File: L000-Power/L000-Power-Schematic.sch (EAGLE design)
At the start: 59 parts, among them IC1 LM7805, IC2 LM7905, IC3 LM7809, IC4 LM7909, X1 JST-XH-2PIN, X10 JST-XH-5PIN, X11 JST-XH-5PIN, X12 JST-XH-5PIN, X13 JST-XH-5PIN, X14 JST-XH-5PIN, X15 JST-XH-5PIN, X16 JST-XH-5PIN, X17 JST-XH-5PIN, X18 JST-XH-5PIN, X19 JST-XH-5PIN, X2 JST-XH-5PIN, X20 JST-XH-5PIN, X21 JST-XH-5PIN, X3 JST-XH-5PIN, X4 JST-XH-5PIN, X5 JST-XH-5PIN, X6 JST-XH-5PIN, X7 JST-XH-5PIN, X8 JST-XH-5PIN, X9 JST-XH-5PIN

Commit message: Power
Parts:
- added R5, R6, R7, R8: 10k, resistor:R-US_0309/10
- C13, C14, C15, C16, C17, C18, C19, C20: device resistor:CPOL-USE5-13 -> rcl:CPOL-USE2,5-6E
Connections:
- new net X1: R8.2
- new net X2: R5.2
- new net X3: R6.2
- new net X4: R7.2
- net 5V+: now also C15.+; no longer C14.+
- net 9V+: now also C19.+; no longer C18.+
- net GND: now also C14.+, C15.-, C18.+, C19.-, R5.1, R6.1, R7.1, R8.1; no longer C14.-, C15.+, C18.-, C19.+
- net N$1: now also C14.-, C18.-; no longer C15.-, C19.-
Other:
- moved on the sheet: C14, C15, C18, C19

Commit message: Power
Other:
- note added: "Panel GND bus"
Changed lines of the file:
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@@
 <sheet>
 <plain>
+<text x="-38.1" y="-99.06" size="1.778" layer="91">Panel GND bus</text>
 </plain>
 <instances>

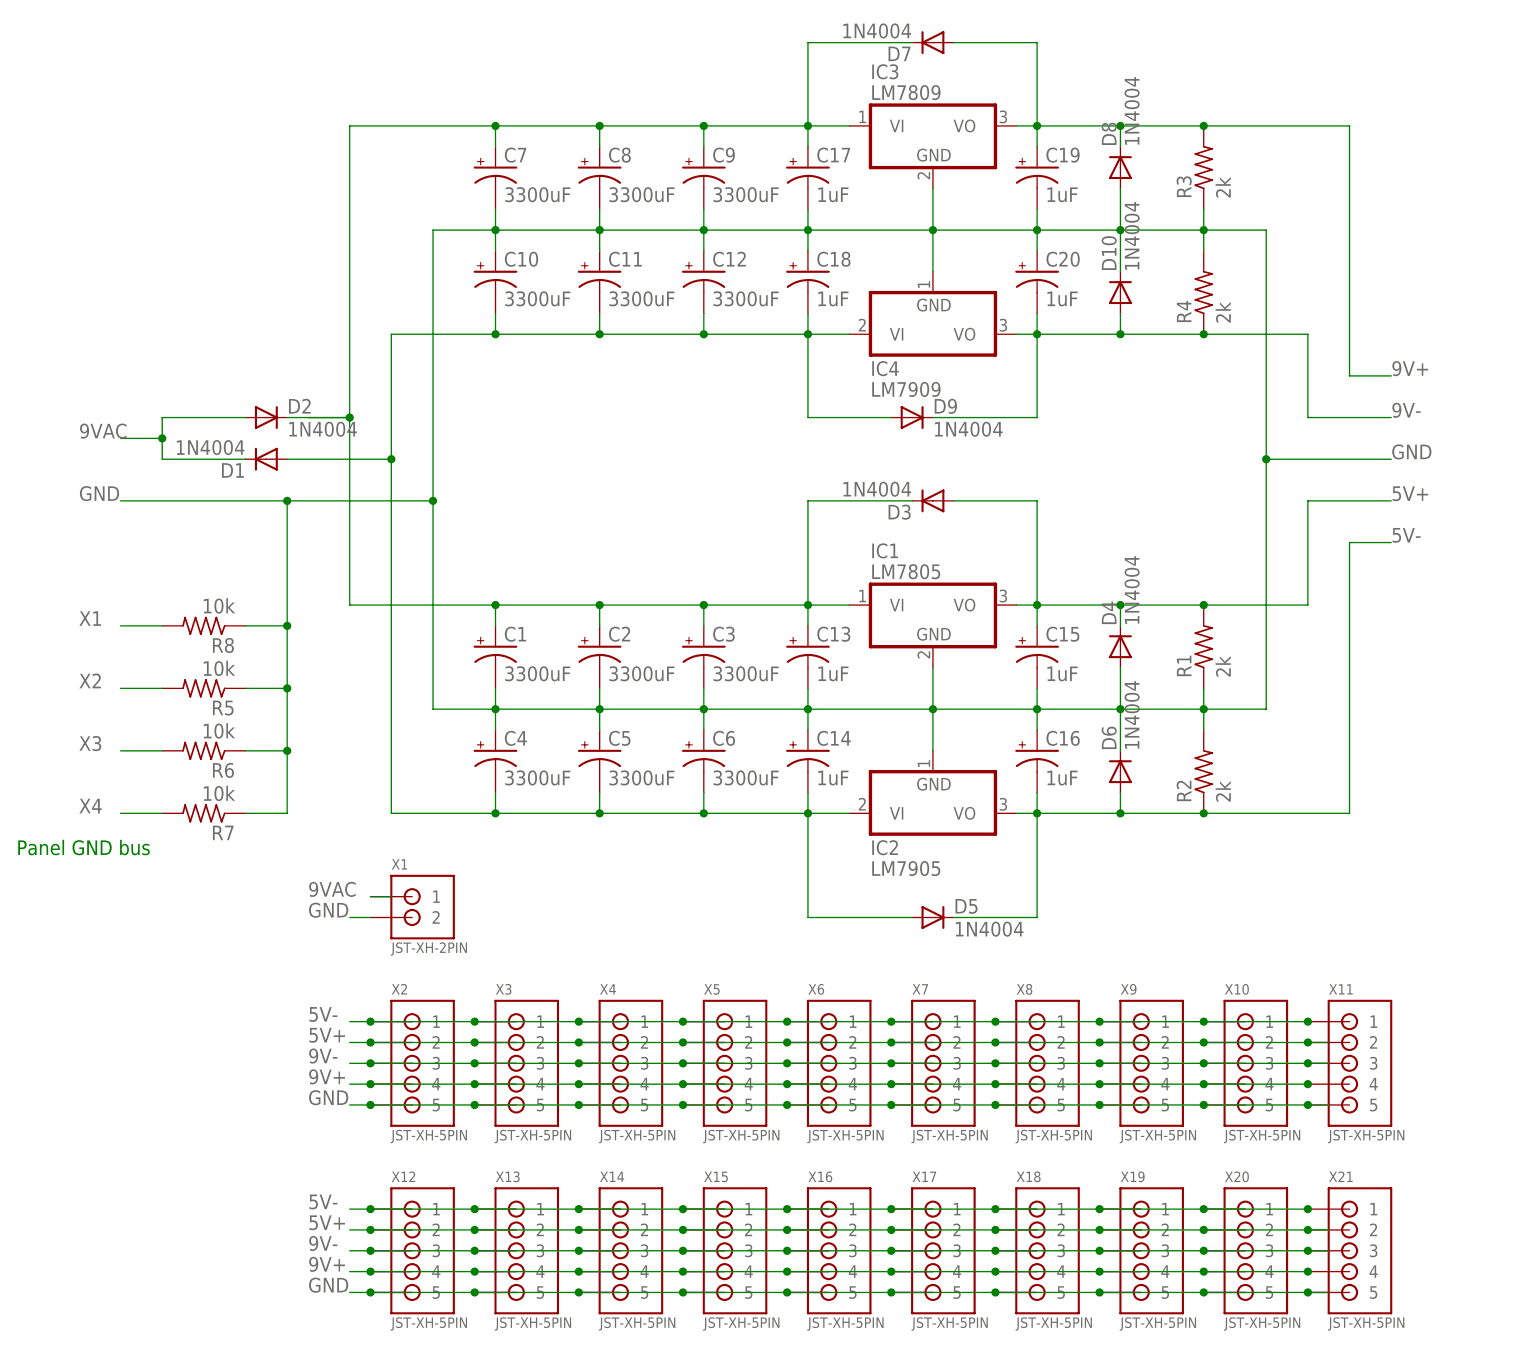
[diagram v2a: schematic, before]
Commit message: Add LEDs
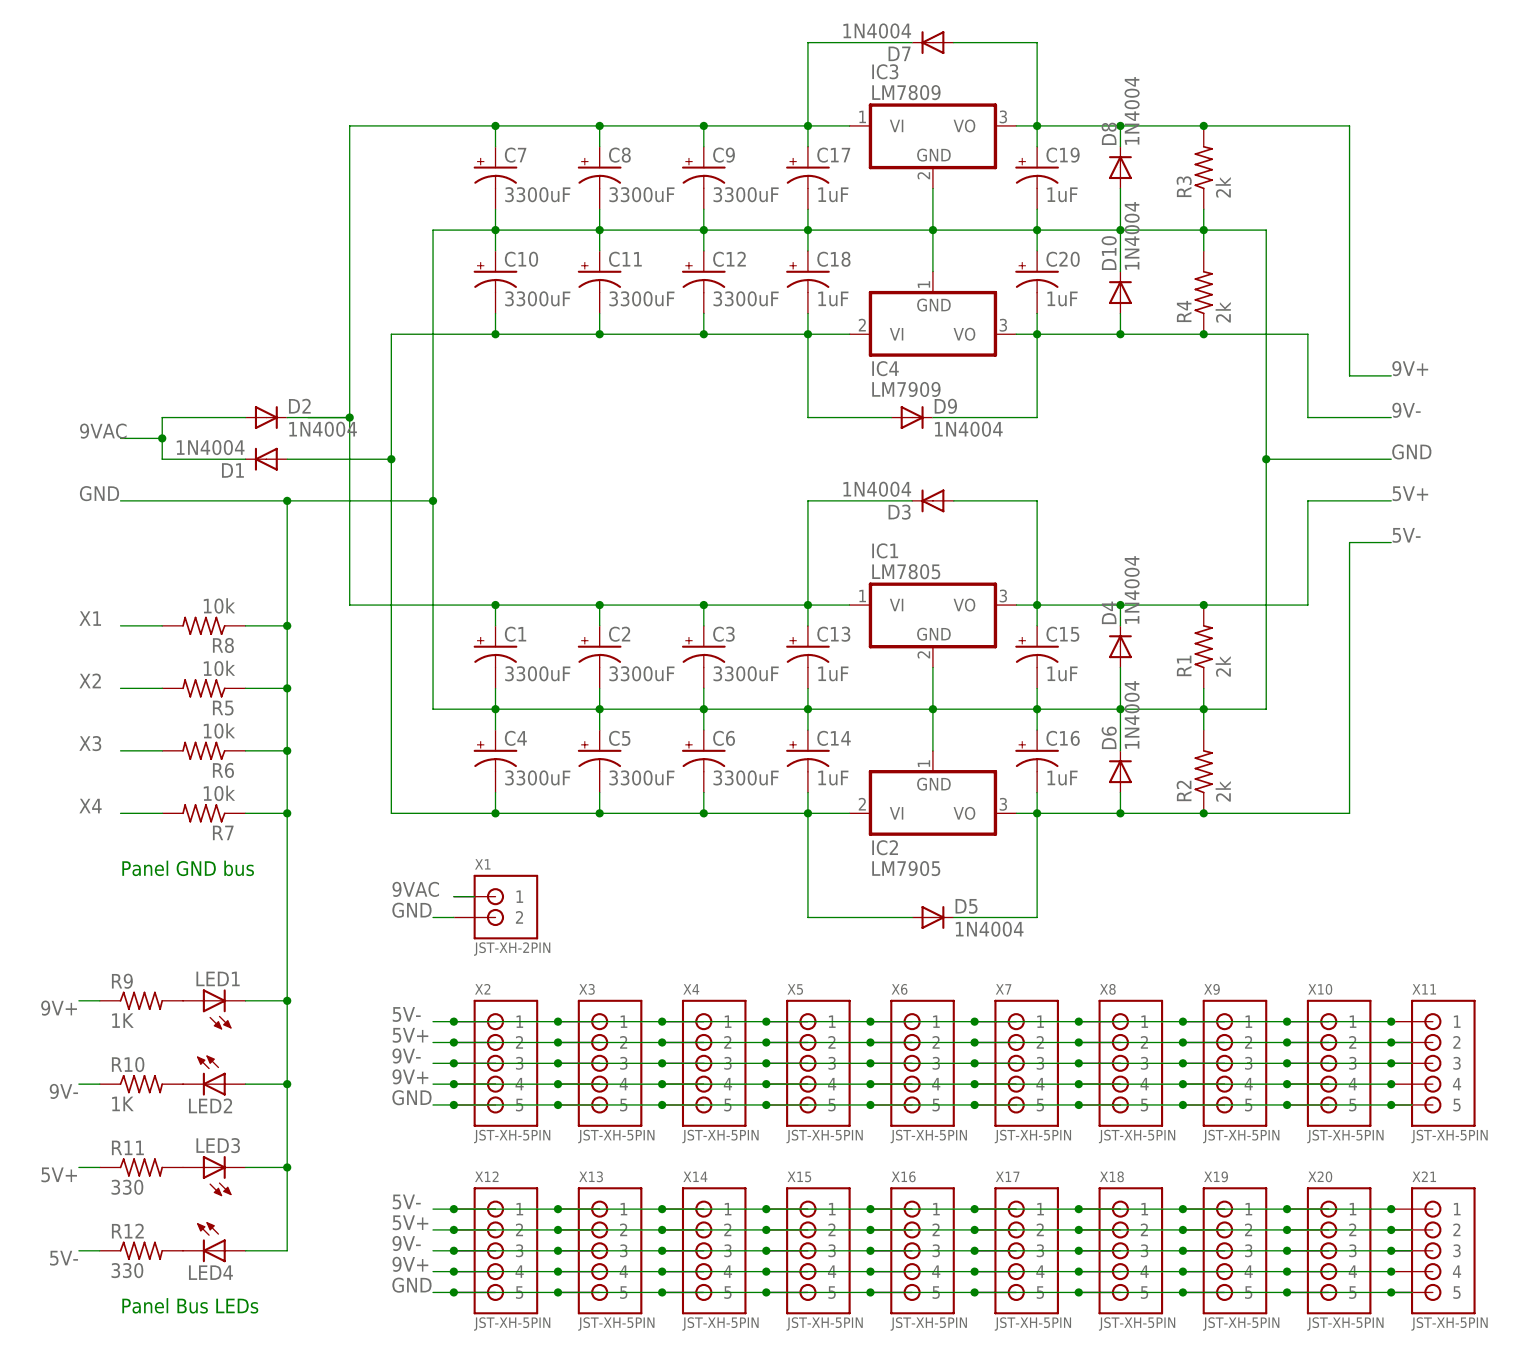
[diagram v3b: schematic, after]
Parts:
- added LED1, LED2, LED3, LED4: (no value), led:LED5MM
- added R10, R9: 1K, resistor:R-US_0309/10
- added R11, R12: 330, resistor:R-US_0309/10
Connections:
- new net N$2: LED3.A, R11.2
- new net N$3: LED4.C, R12.2
- new net N$4: LED1.A, R9.2
- new net N$5: LED2.C, R10.2
- net 5V+: now also R11.1
- net 5V-: now also R12.1
- net 9V+: now also R9.1
- net 9V-: now also R10.1
- net GND: now also LED1.C, LED2.A, LED3.C, LED4.A
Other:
- note added: "Panel Bus LEDs"
- moved on the sheet: X1, X10, X11, X12, X13, X14, X15, X16, X17, X18, X19, X2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

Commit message: FIX V2
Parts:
- removed C15, C16, C17, C18, C19, C20: 1uF, rcl:CPOL-USE2,5-6E
- removed R5, R6, R7, R8: 10k, resistor:R-US_0309/10
- C10, C11, C12, C7, C8, C9: value 3300uF -> 1uF; device resistor:CPOL-USE5-13 -> rcl:CPOL-USE2,5-6E
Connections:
- removed net N$1: C10.-, C11.-, C12.-, C14.-, C18.-, C4.-, C5.-, C6.-, D1.A, D5.A, D9.A, IC2.VI, IC4.VI
- removed net N$8: C1.+, C13.+, C17.+, C2.+, C3.+, C7.+, C8.+, C9.+, D2.C, D3.C, D7.C, IC1.VI, IC3.VI
- removed net X1: R8.2
- removed net X2: R5.2
- removed net X3: R6.2
- removed net X4: R7.2
- new net N$14: C13.-, C4.-, C5.-, C6.-, C9.-, D5.A, D9.A, IC2.VI, IC4.VI
- new net N$7: C1.+, C11.+, C2.+, C3.+, C7.+, D2.C, D3.C, D7.C, IC1.VI, IC3.VI
- net 5V+: now also C12.+; no longer C15.+
- net 5V-: now also C14.-; no longer C16.-
- net 9V+: now also C8.+; no longer C19.+
- net 9V-: now also C10.-; no longer C20.-
- net GND: now also C11.-, C12.-, C13.+, C9.+; no longer C11.+, C12.+, C13.-, C15.-, C16.+, C17.-, C18.+, C19.-, C20.+, C9.-, R5.1, R6.1, R7.1, R8.1
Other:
- note added: "X1"
- note added: "X2"
- note added: "X3"
- note added: "X4"
- moved on the sheet: C1, C10, C11, C12, C13, C14, C2, C3, C4, C5, C6, C7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

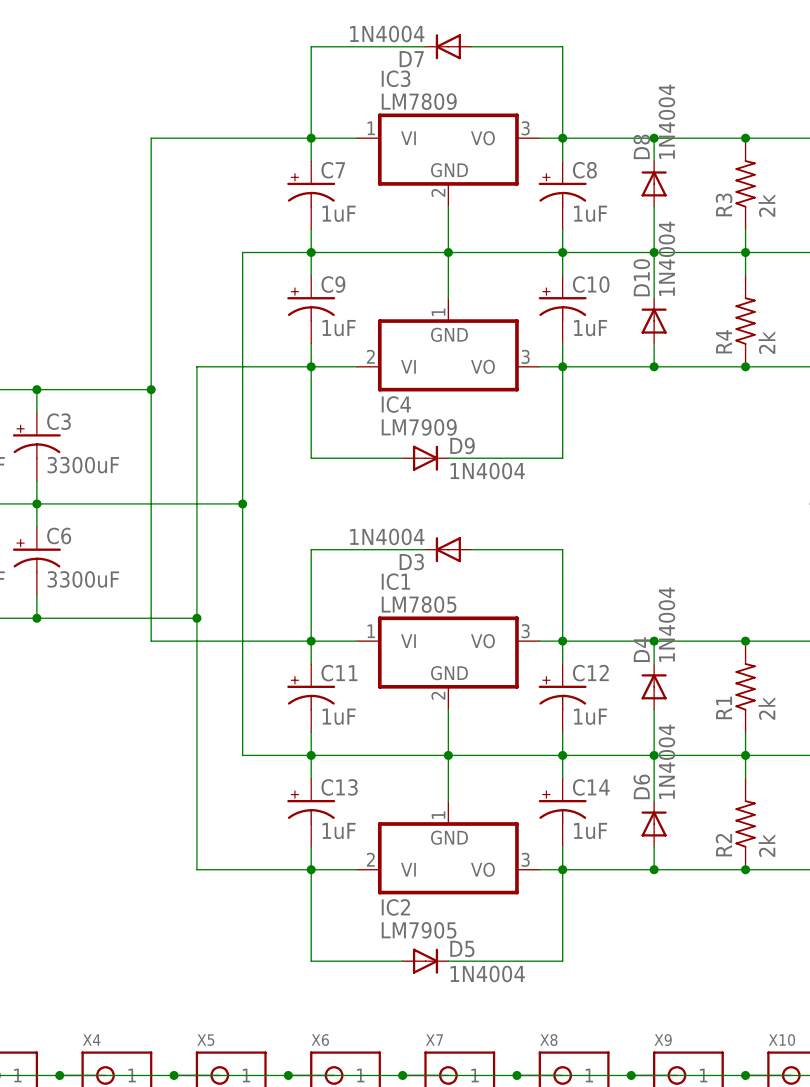
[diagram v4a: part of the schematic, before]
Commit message: POWER
Updated schematic and start of strip board
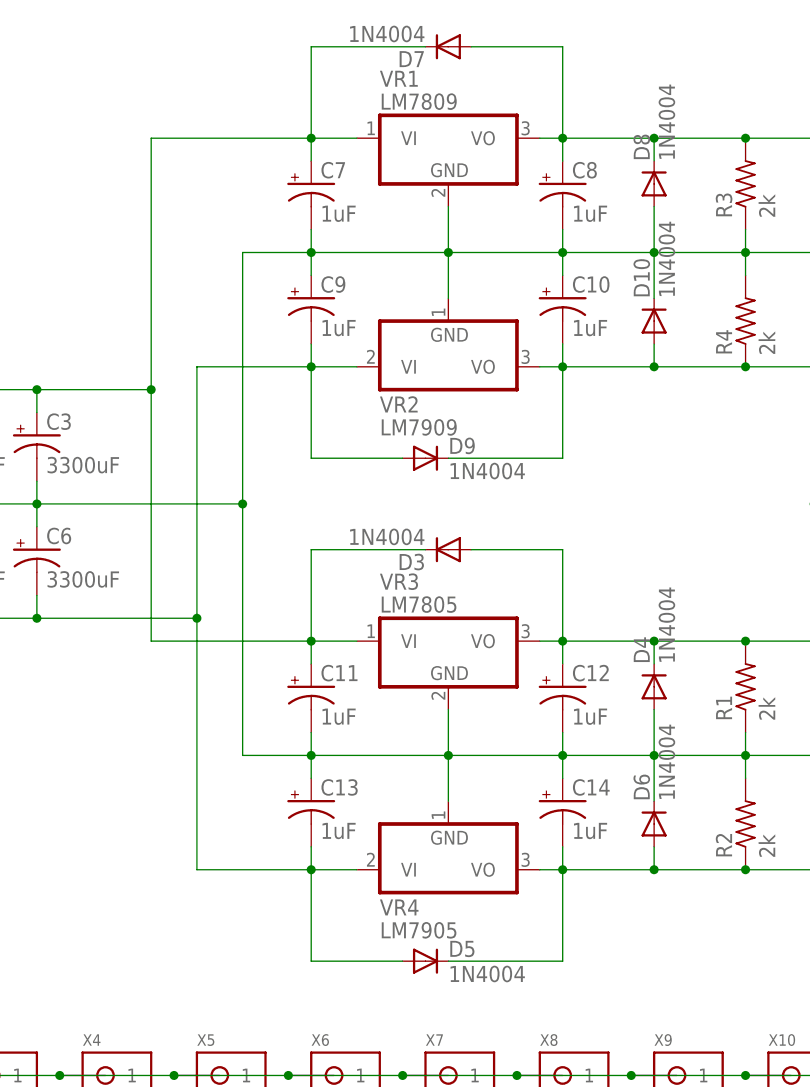
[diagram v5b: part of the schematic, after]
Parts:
- renumbered IC1 to VR3, IC2 to VR4, IC3 to VR1, IC4 to VR2
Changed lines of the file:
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@@
 <part name="C5" library="resistor" deviceset="CPOL-US" device="E5-13" value="3300uF"/>
 <part name="C6" library="resistor" deviceset="CPOL-US" device="E5-13" value="3300uF"/>
-<part name="IC1" library="linear" deviceset="78*" device="T" technology="05" value="LM7805"/>
+<part name="VR3" library="linear" deviceset="78*" device="T" technology="05" value="LM7805"/>
 <part name="D1" library="diode" deviceset="1N4004" device=""/>
 <part name="D2" library="diode" deviceset="1N4004" device=""/>
@@
 <part name="D5" library="diode" deviceset="1N4004" device=""/>
 <part name="D6" library="diode" deviceset="1N4004" device=""/>
-<part name="IC2" library="linear" deviceset="79*" device="T" technology="05" value="LM7905"/>
-<part name="IC3" library="linear" deviceset="78*" device="T" technology="08" value="LM7809"/>
-<part name="IC4" library="linear" deviceset="79*" device="T" technology="08" value="LM7909"/>
+<part name="VR4" library="linear" deviceset="79*" device="T" technology="05" value="LM7905"/>
+<part name="VR1" library="linear" deviceset="78*" device="T" technology="08" value="LM7809"/>
+<part name="VR2" library="linear" deviceset="79*" device="T" technology="08" value="LM7909"/>
 <part name="D7" library="diode" deviceset="1N4004" device=""/>
 <part name="D8" library="diode" deviceset="1N4004" device=""/>
@@
 <instance part="C5" gate="G$1" x="22.86" y="-55.88"/>
 <instance part="C6" gate="G$1" x="35.56" y="-55.88"/>
-<instance part="IC1" gate="A1" x="81.28" y="-66.04"/>
+<instance part="VR3" gate="A1" x="81.28" y="-66.04"/>
 <instance part="D1" gate="1" x="-7.62" y="-50.8" rot="R180"/>
 <instance part="D2" gate="1" x="-7.62" y="-45.72"/>
@@
 <instance part="D5" gate="1" x="78.74" y="-101.6"/>
 <instance part="D6" gate="1" x="104.14" y="-86.36" rot="R90"/>
-<instance part="IC2" gate="A1" x="81.28" y="-88.9"/>
-<instance part="IC3" gate="A1" x="81.28" y="-10.16"/>
-<instance part="IC4" gate="A1" x="81.28" y="-33.02"/>
+<instance part="VR4" gate="A1" x="81.28" y="-88.9"/>
+<instance part="VR1" gate="A1" x="81.28" y="-10.16"/>
+<instance part="VR2" gate="A1" x="81.28" y="-33.02"/>
 <instance part="D7" gate="1" x="81.28" y="0" rot="R180"/>
 <instance part="D8" gate="1" x="104.14" y="-15.24" rot="R90"/>
@@
 <wire x1="58.42" y1="-50.8" x2="58.42" y2="-78.74" width="0.1524" layer="91"/>
 <junction x="58.42" y="-50.8"/>
-<pinref part="IC2" gate="A1" pin="GND"/>
+<pinref part="VR4" gate="A1" pin="GND"/>
 <pinref part="C14" gate="G$1" pin="+"/>
 <pinref part="D10" gate="1" pin="C"/>
 <pinref part="C10" gate="G$1" pin="+"/>
-<pinref part="IC4" gate="A1" pin="GND"/>
+<pinref part="VR2" gate="A1" pin="GND"/>
 <pinref part="C9" gate="G$1" pin="+"/>
 <pinref part="C7" gate="G$1" pin="-"/>
@@
 <wire x1="66.04" y1="-22.86" x2="66.04" y2="-25.4" width="0.1524" layer="91"/>
 <wire x1="66.04" y1="-22.86" x2="81.28" y2="-22.86" width="0.1524" layer="91"/>
-<pinref part="IC3" gate="A1" pin="GND"/>
+<pinref part="VR1" gate="A1" pin="GND"/>
 <wire x1="81.28" y1="-17.78" x2="81.28" y2="-22.86" width="0.1524" layer="91"/>
 <junction x="81.28" y="-22.86"/>
@@
 <junction x="81.28" y="-78.74"/>
 <wire x1="81.28" y1="-78.74" x2="81.28" y2="-83.82" width="0.1524" layer="91"/>
-<pinref part="IC1" gate="A1" pin="GND"/>
+<pinref part="VR3" gate="A1" pin="GND"/>
 <wire x1="81.28" y1="-73.66" x2="81.28" y2="-78.74" width="0.1524" layer="91"/>
 <pinref part="C11" gate="G$1" pin="-"/>
@@
 <wire x1="104.14" y1="-66.04" x2="114.3" y2="-66.04" width="0.1524" layer="91"/>
 <wire x1="104.14" y1="-66.04" x2="104.14" y2="-68.58" width="0.1524" layer="91"/>
-<pinref part="IC1" gate="A1" pin="VO"/>
+<pinref part="VR3" gate="A1" pin="VO"/>
 <wire x1="91.44" y1="-66.04" x2="93.98" y2="-66.04" width="0.1524" layer="91"/>
 <junction x="104.14" y="-66.04"/>
@@
 <net name="5V-" class="0">
 <segment>
-<pinref part="IC2" gate="A1" pin="VO"/>
+<pinref part="VR4" gate="A1" pin="VO"/>
 <wire x1="91.44" y1="-91.44" x2="93.98" y2="-91.44" width="0.1524" layer="91"/>
 <pinref part="R2" gate="G$1" pin="1"/>
@@
 <net name="9V+" class="0">
 <segment>
-<pinref part="IC3" gate="A1" pin="VO"/>
+<pinref part="VR1" gate="A1" pin="VO"/>
 <wire x1="91.44" y1="-10.16" x2="93.98" y2="-10.16" width="0.1524" layer="91"/>
 <wire x1="93.98" y1="-10.16" x2="104.14" y2="-10.16" width="0.1524" layer="91"/>
@@
 <net name="9V-" class="0">
 <segment>
-<pinref part="IC4" gate="A1" pin="VO"/>
+<pinref part="VR2" gate="A1" pin="VO"/>
 <wire x1="91.44" y1="-35.56" x2="93.98" y2="-35.56" width="0.1524" layer="91"/>
 <wire x1="93.98" y1="-35.56" x2="104.14" y2="-35.56" width="0.1524" layer="91"/>
@@
 <junction x="35.56" y="-63.5"/>
 <wire x1="53.34" y1="-63.5" x2="53.34" y2="-35.56" width="0.1524" layer="91"/>
-<pinref part="IC4" gate="A1" pin="VI"/>
+<pinref part="VR2" gate="A1" pin="VI"/>
 <pinref part="C9" gate="G$1" pin="-"/>
 <wire x1="66.04" y1="-33.02" x2="66.04" y2="-35.56" width="0.1524" layer="91"/>
@@
 <pinref part="D5" gate="1" pin="A"/>
 <wire x1="66.04" y1="-101.6" x2="76.2" y2="-101.6" width="0.1524" layer="91"/>
-<pinref part="IC2" gate="A1" pin="VI"/>
+<pinref part="VR4" gate="A1" pin="VI"/>
 <wire x1="71.12" y1="-91.44" x2="66.04" y2="-91.44" width="0.1524" layer="91"/>
 <junction x="66.04" y="-91.44"/>
@@
 <net name="N$7" class="0">
 <segment>
-<pinref part="IC3" gate="A1" pin="VI"/>
+<pinref part="VR1" gate="A1" pin="VI"/>
 <wire x1="71.12" y1="-10.16" x2="66.04" y2="-10.16" width="0.1524" layer="91"/>
 <junction x="66.04" y="-10.16"/>
@@
 <wire x1="48.26" y1="-38.1" x2="48.26" y2="-66.04" width="0.1524" layer="91"/>
 <junction x="48.26" y="-38.1"/>
-<pinref part="IC1" gate="A1" pin="VI"/>
+<pinref part="VR3" gate="A1" pin="VI"/>
 <wire x1="71.12" y1="-66.04" x2="66.04" y2="-66.04" width="0.1524" layer="91"/>
 <junction x="66.04" y="-66.04"/>

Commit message: Power schematic update
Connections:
- net 5V+: now also D7.A, D8.C, R3.2; no longer D3.A, D4.C, R1.2
- net 5V-: now also D10.A, D9.C, R4.1; no longer D5.C, D6.A, R2.1
- net 9V+: now also D3.A, D4.C, R1.2; no longer D7.A, D8.C, R3.2
- net 9V-: now also D5.C, D6.A, R2.1; no longer D10.A, D9.C, R4.1
- net N$14: now also D1.A
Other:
- moved on the sheet: C10, C11, C12, C13, C14, C7, C8, C9, D10, D3, D4, D5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

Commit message: Final
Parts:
- R10, R9: value 1K -> 220K
- R11, R12: value 330 -> 120K
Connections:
- net 5V+: now also X10.4, X11.4, X12.4, X13.4, X14.4, X15.4, X16.4, X17.4, X18.4, X19.4, X2.4, X20.4, X21.4, X3.4, X4.4, X5.4, X6.4, X7.4, X8.4, X9.4; no longer X10.2, X11.2, X12.2, X13.2, X14.2, X15.2, X16.2, X17.2, X18.2, X19.2, X2.2, X20.2, X21.2, X3.2, X4.2, X5.2, X6.2, X7.2, X8.2, X9.2
- net 5V-: now also X10.2, X11.2, X12.2, X13.2, X14.2, X15.2, X16.2, X17.2, X18.2, X19.2, X2.2, X20.2, X21.2, X3.2, X4.2, X5.2, X6.2, X7.2, X8.2, X9.2; no longer X10.1, X11.1, X12.1, X13.1, X14.1, X15.1, X16.1, X17.1, X18.1, X19.1, X2.1, X20.1, X21.1, X3.1, X4.1, X5.1, X6.1, X7.1, X8.1, X9.1
- net 9V+: now also X10.5, X11.5, X12.5, X13.5, X14.5, X15.5, X16.5, X17.5, X18.5, X19.5, X2.5, X20.5, X21.5, X3.5, X4.5, X5.5, X6.5, X7.5, X8.5, X9.5; no longer X10.4, X11.4, X12.4, X13.4, X14.4, X15.4, X16.4, X17.4, X18.4, X19.4, X2.4, X20.4, X21.4, X3.4, X4.4, X5.4, X6.4, X7.4, X8.4, X9.4
- net 9V-: now also X10.1, X11.1, X12.1, X13.1, X14.1, X15.1, X16.1, X17.1, X18.1, X19.1, X2.1, X20.1, X21.1, X3.1, X4.1, X5.1, X6.1, X7.1, X8.1, X9.1; no longer X10.3, X11.3, X12.3, X13.3, X14.3, X15.3, X16.3, X17.3, X18.3, X19.3, X2.3, X20.3, X21.3, X3.3, X4.3, X5.3, X6.3, X7.3, X8.3, X9.3
- net GND: now also X10.3, X11.3, X12.3, X13.3, X14.3, X15.3, X16.3, X17.3, X18.3, X19.3, X2.3, X20.3, X21.3, X3.3, X4.3, X5.3, X6.3, X7.3, X8.3, X9.3; no longer X10.5, X11.5, X12.5, X13.5, X14.5, X15.5, X16.5, X17.5, X18.5, X19.5, X2.5, X20.5, X21.5, X3.5, X4.5, X5.5, X6.5, X7.5, X8.5, X9.5
